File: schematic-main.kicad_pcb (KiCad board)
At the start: 2 copper layers, 107 parts, among them IC1 AD8544ARUZ-REEL, IC2 LM76202QPWPRQ1, J1 Battery, J2 CAN, J3 V_P, J7 C_P, J8 VALVE, J9 PURGE_VALVE, P1 USB_C_Plug_USB2.0, T1 PMPB15XP_115, U2 TPS62933, U3 USBLC6-2P6, U4 ESP32-S3FN8, U5 SN65HVD232, Y1 Crystal_GND24

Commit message: Drawing PCB
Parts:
- moved R26 200.8 mm to (70.4, 158.5), turned to -90 degrees
- moved IC1 196.7 mm to (76.5, 157.7), turned to 180 degrees
- moved U2 193.4 mm to (68.5, 107.8)
- moved D2 192.2 mm to (64.6, 100.9), turned to 90 degrees
- moved R22 187.5 mm to (73.8, 83.2), turned to 180 degrees
- moved L1 186.3 mm to (76.0, 107.5), turned to 90 degrees
- moved R9 182.0 mm to (69.6, 96.4), turned to 180 degrees
- moved R17 180.9 mm to (83.3, 151.1), turned to 90 degrees
- moved R29 180.1 mm to (94.5, 138.2), turned to 90 degrees
- moved C30 179.8 mm to (73.6, 152.2), turned to 90 degrees
- moved C3 178.0 mm to (65.2, 109.5), turned to -90 degrees
- moved R16 176.6 mm to (84.8, 155.0), turned to 180 degrees
- moved D6 176.5 mm to (79.2, 83.2)
- moved R7 175.9 mm to (74.6, 96.4), turned to 180 degrees
- moved C26 175.4 mm to (79.4, 152.2), turned to 90 degrees
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- renumbered T1 to MOSFET1
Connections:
- D3 pad 1: /IO/CANH -> /IO/CANL
- D3 pad 2: /IO/CANL -> /IO/CANH
- U4 pad 12: /I/O_1_MCU -> unconnected-(U4-GPIO7/ADC1_CH6-Pad12)
- U4 pad 13: /I/O_2_MCU -> unconnected-(U4-GPIO8/ADC1_CH7-Pad13)
- U4 pad 14: /I/O_3_MCU -> unconnected-(U4-GPIO9/ADC1_CH8-Pad14)
- U4 pad 15: /I/O_4_MCU -> unconnected-(U4-GPIO10/ADC1_CH9-Pad15)
- U4 pad 18: /V_P_MCU -> unconnected-(U4-GPIO13/ADC2_CH2-Pad18)
- U4 pad 19: /PURGE_VALVE_MCU -> unconnected-(U4-GPIO14/ADC2_CH3-Pad19)
- U4 pad 23: unconnected-(U4-GPIO17/ADC2_CH6-Pad23) -> /V_P_MCU
- U4 pad 24: unconnected-(U4-GPIO18/ADC2_CH7-Pad24) -> /C_P_MCU
- U4 pad 39: unconnected-(U4-GPIO34-Pad39) -> /I/O_1_MCU
- U4 pad 40: unconnected-(U4-GPIO35-Pad40) -> /I/O_2_MCU
- U4 pad 41: unconnected-(U4-GPIO36-Pad41) -> /I/O_3_MCU
- U4 pad 42: unconnected-(U4-GPIO37-Pad42) -> /I/O_4_MCU
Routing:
- net GND: track 0.00 -> 604.2 mm, vias 0 -> 57
- net +12V: track 0.00 -> 274.8 mm
- net +3.3V: track 0.00 -> 248.3 mm, vias 0 -> 7
- net /MCU/MCU_TEST: track 0.00 -> 100.5 mm, vias 0 -> 2
- net /MCU/BOOT: track 0.00 -> 95.2 mm, vias 0 -> 2
- net /VBUS: track 0.00 -> 95.1 mm, vias 0 -> 2
- net /MCU/RESET: track 0.00 -> 90.4 mm, vias 0 -> 2
- net /MCU/USB_D+: track 0.00 -> 58.7 mm, vias 0 -> 2
- net /MCU/USB_D-: track 0.00 -> 56.7 mm
- net /I/O_4_MCU: track 0.00 -> 47.4 mm, vias 0 -> 2
- net /I/O_3_MCU: track 0.00 -> 42.2 mm, vias 0 -> 2
- net /IO/VALVE: track 0.00 -> 39.3 mm
- net /IO/PURGE_VALVE: track 0.00 -> 39.1 mm
- net /I/O_2_MCU: track 0.00 -> 37.5 mm, vias 0 -> 2
- net +5V: track 0.00 -> 37.0 mm
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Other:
- board outline added: 102.3 x 135.4 mm
- board text added: "12V"
- board text added: "3.3V"
- board text added: "5V"
- board text added: "BOOT"
- board text added: "CAN_STATUS"
- board text added: "GND"
- board text added: "I/O_1"
- board text added: "I/O_2"
- board text added: "I/O_3"
- board text added: "I/O_4"
- board text added: "MCU_STATUS"
- board text added: "MCU_TEST"
- board text added: "RESET"

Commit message: Makin GND sphere
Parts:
- added H1: MountingHole, MountingHole:MountingHole_3.2mm_M3_DIN965, F.Cu at (146.8, 51.8)
- added H2: MountingHole, MountingHole:MountingHole_3.2mm_M3_DIN965, F.Cu at (53.6, 51.8)
- added H3: MountingHole, MountingHole:MountingHole_3.2mm_M3_DIN965, F.Cu at (53.4, 178.4)
- added H4: MountingHole, MountingHole:MountingHole_3.2mm_M3_DIN965, F.Cu at (146.8, 178.6)
- moved C25 7.80 mm to (139.7, 177.6)
- moved JP3 7.80 mm to (140.4, 180.4)
- moved R23 7.80 mm to (139.8, 174.9)
- moved C13 4.60 mm to (133.0, 177.6)
- moved JP2 4.60 mm to (133.9, 180.4)
- moved R13 4.60 mm to (133.0, 174.9)
- moved TP3 3.20 mm to (141.2, 59.4)
- moved TP4 3.20 mm to (148.1, 59.4)
- moved C12 2.47 mm to (126.2, 177.6)
- moved R12 2.47 mm to (126.2, 174.9)
- moved JP1 2.47 mm to (127.0, 180.5)
- moved C10 1.50 mm to (105.8, 114.8)
- moved TP5 1.50 mm to (141.1, 65.2)
- moved TP6 1.50 mm to (148.1, 65.2)
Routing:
- net /C_P_MCU: track 2.74 -> 73.2 mm, vias 0 -> 2
- net /V_P_MCU: track 2.74 -> 67.7 mm, vias 0 -> 2
- net /MCU/MCU_TEST: track 100.5 -> 93.6 mm
- net GND: track 604.2 -> 609.7 mm, vias 57 -> 59
- net /MCU/BOOT: track 95.2 -> 90.8 mm
- net +3.3V: track 248.3 -> 251.2 mm, vias 7 -> 10
- net +12V: track 274.8 -> 272.0 mm
- net /MCU/RESET: track 90.4 -> 89.6 mm
- net +5V: track 37.0 -> 36.4 mm
- added copper zone on B.Cu, net GND
- added copper zone on F.Cu, net GND

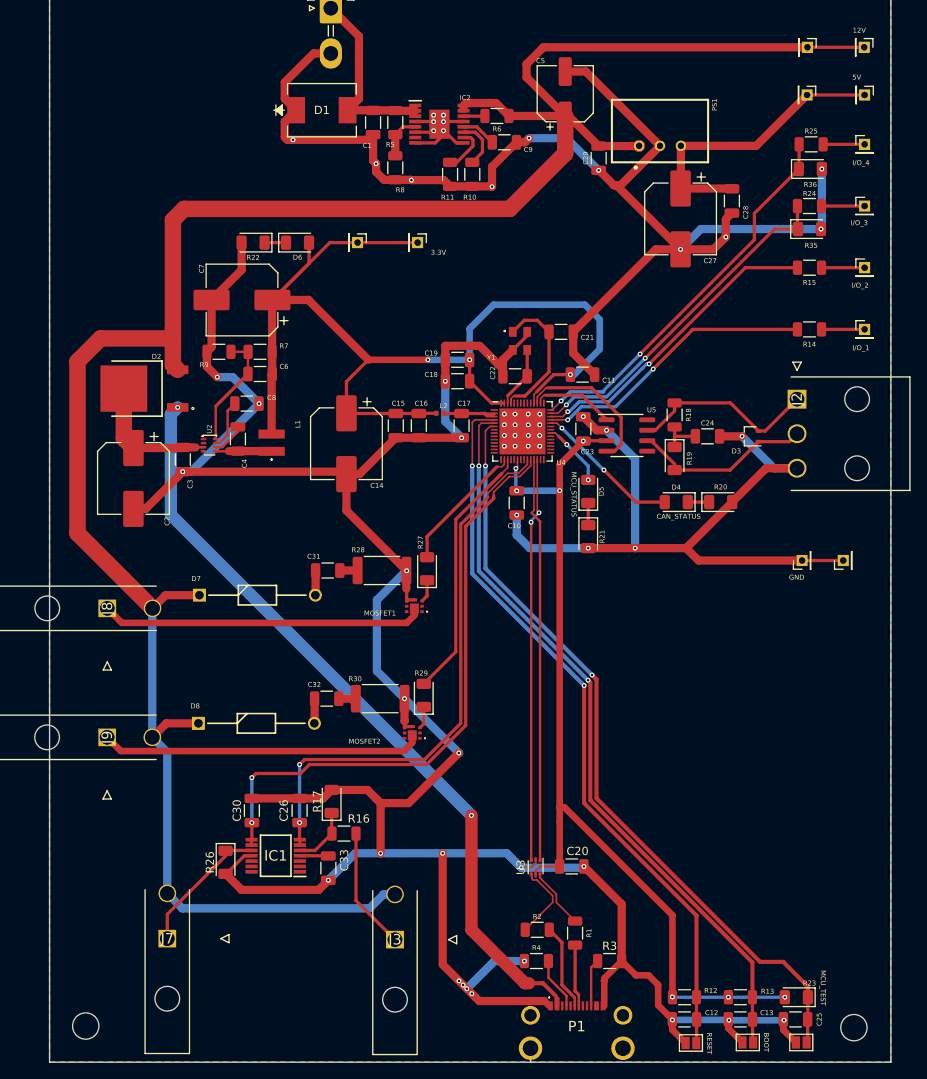
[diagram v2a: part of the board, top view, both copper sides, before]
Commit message: Adding connector for Hydrogen Sensor
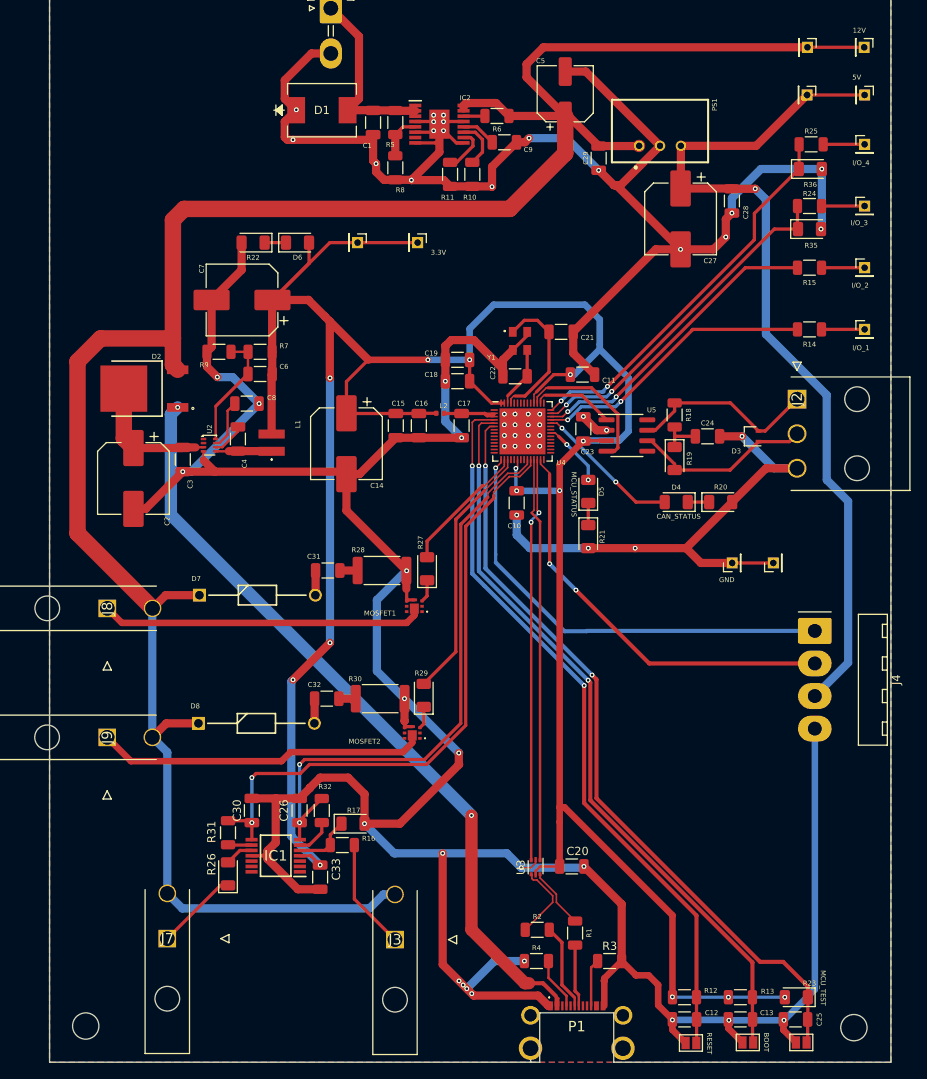
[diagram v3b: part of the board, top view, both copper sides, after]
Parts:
- added J4: Conn_01x04, Connector_Molex:Molex_KK-396_A-41792-0004_1x04_P3.96mm_Horizontal, F.Cu at (142.0, 130.4)
- added R31: 1k, Resistor_SMD:R_1206_3216Metric, F.Cu at (70.7, 154.9)
- added R32: 1k, Resistor_SMD:R_1206_3216Metric, F.Cu at (82.1, 152.2)
- R16: value 10k -> 5k
- R17: value 5k -> 10k
- R26: value 100R -> 150R
- moved TP1 8.51 mm to (132.0, 122.1)
- moved TP2 8.51 mm to (137.0, 122.1)
- moved R17 3.75 mm to (85.9, 153.8), turned to 0 degrees
- moved C33 1.49 mm to (81.9, 160.3)
- moved R26 1.43 mm to (70.7, 159.9), turned to 90 degrees
- moved R16 1.41 mm to (84.6, 156.4)
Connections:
- net /IO/V_P renamed /IO/PRESSURE_SENSOR_V
- C26 pad 1: /V_P_MCU -> /PRESSURE_SENSOR_V_MCU
- C30 pad 1: /C_P_MCU -> /PRESSURE_SENSOR_I_MCU
- IC1 pad 10: /IO/C_P -> Net-(IC1-+IN_C)
- IC1 pad 6: /V_P_MCU -> Net-(IC1--IN_B)
- IC1 pad 7: /V_P_MCU -> /PRESSURE_SENSOR_V_MCU
- IC1 pad 8: /C_P_MCU -> /PRESSURE_SENSOR_I_MCU
- IC1 pad 9: /C_P_MCU -> Net-(IC1--IN_C)
- J7 pad 1: /IO/C_P -> /IO/PRESSURE_SENSOR_I
- R26 pad 1: /IO/C_P -> /IO/PRESSURE_SENSOR_I
- R26 pad 2: GND -> Net-(IC1-+IN_C)
- U4 pad 15: unconnected-(U4-GPIO10/ADC1_CH9-Pad15) -> /HYDROGEN_SENSOR_ADC
- U4 pad 23: /V_P_MCU -> /PRESSURE_SENSOR_V_MCU
- U4 pad 24: /C_P_MCU -> /PRESSURE_SENSOR_I_MCU
- U4 pad 27: unconnected-(U4-GPIO21-Pad27) -> /HYDROGEN_SENSOR_
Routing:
- net +3.3V: track 251.2 -> 337.5 mm, vias 10 -> 14
- net /PRESSURE_SENSOR_I_MCU: track 0.00 -> 75.5 mm, vias 0 -> 2
- net /C_P_MCU: track 73.2 -> 0.00 mm, vias 2 -> 0
- net /PRESSURE_SENSOR_V_MCU: track 0.00 -> 71.1 mm, vias 0 -> 2
- net +5V: track 36.4 -> 107.2 mm, vias 0 -> 1
- net /V_P_MCU: track 67.7 -> 0.00 mm, vias 2 -> 0
- net /HYDROGEN_SENSOR_ADC: track 0.00 -> 55.1 mm, vias 0 -> 1
- net /HYDROGEN_SENSOR_: track 0.00 -> 50.4 mm, vias 0 -> 2
- net GND: track 609.7 -> 627.8 mm, vias 59 -> 60
- net /IO/C_P: track 16.8 -> 0.00 mm
- net /IO/PRESSURE_SENSOR_I: track 0.00 -> 10.1 mm
- net Net-(IC1--IN_B): track 0.00 -> 4.51 mm
- net Net-(IC1-+IN_C): track 0.00 -> 3.46 mm
- net Net-(IC1--IN_C): track 0.00 -> 2.88 mm
- net /IO/PRESSURE_SENSOR_V: track 14.9 -> 13.5 mm
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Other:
- outline, holes or cut-outs redrawn

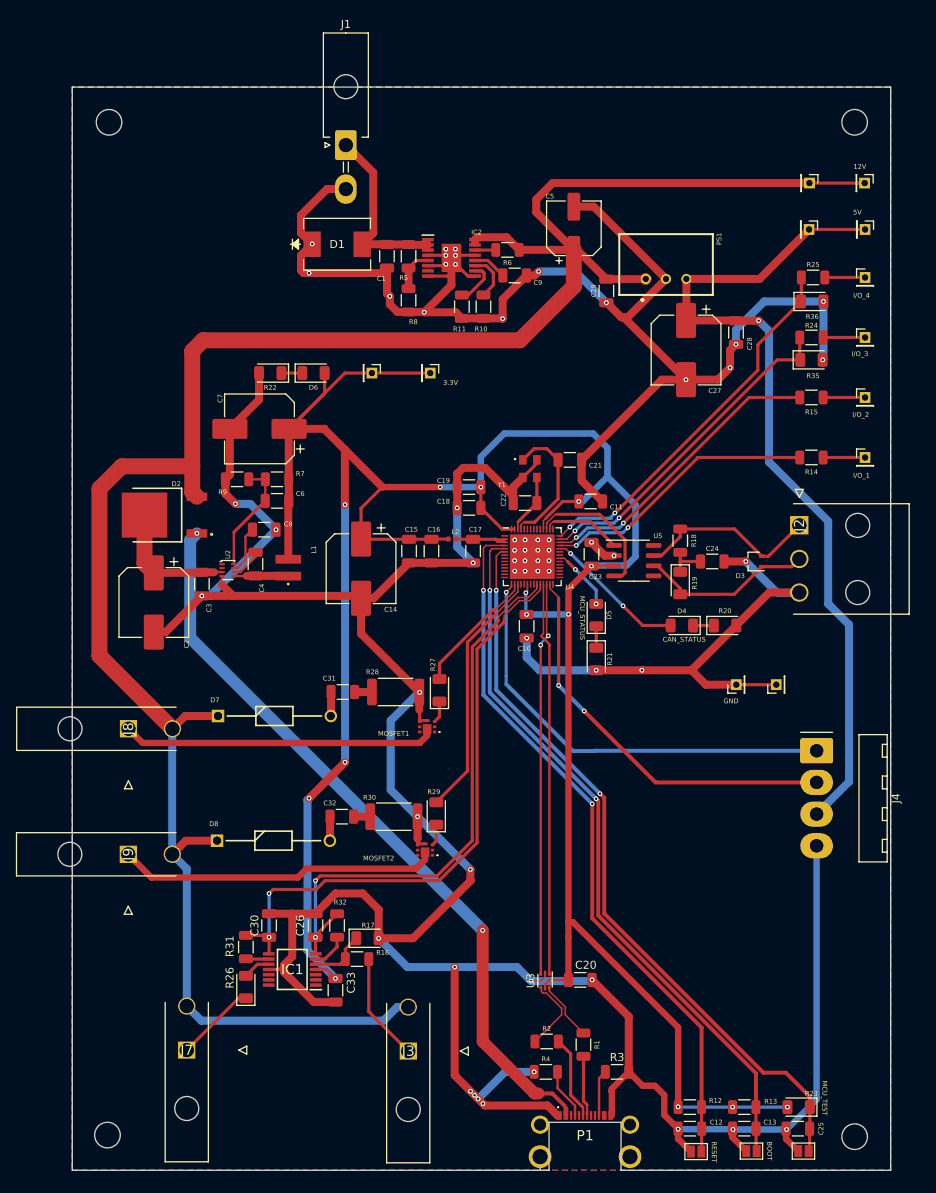
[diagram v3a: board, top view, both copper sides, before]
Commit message: Adding motor driver unit
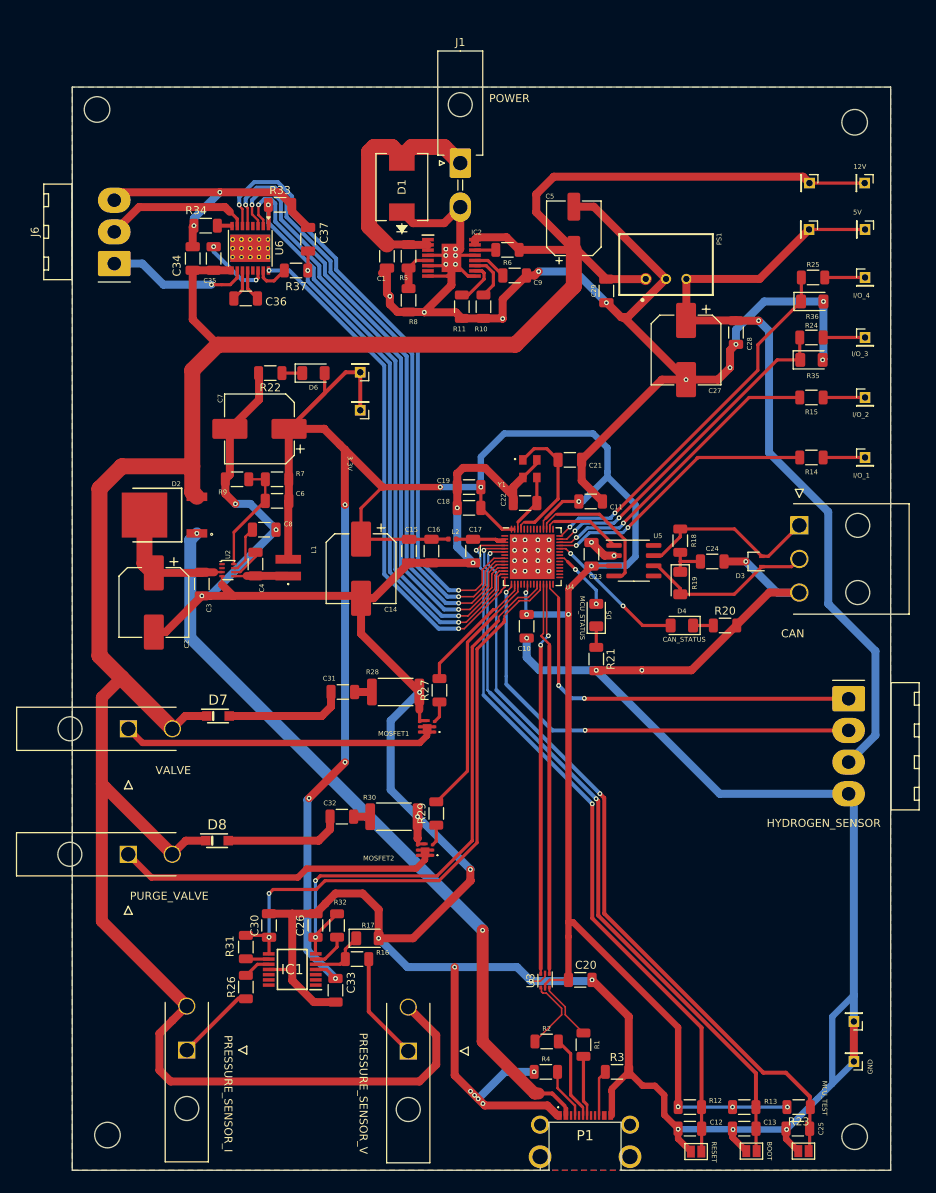
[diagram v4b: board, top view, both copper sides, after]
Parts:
- added C34: 100n, Capacitor_SMD:C_1206_3216Metric, F.Cu at (64.1, 68.8)
- added C35: 100n, Capacitor_SMD:C_1206_3216Metric, F.Cu at (66.7, 68.8)
- added C36: 100n, Capacitor_SMD:C_1206_3216Metric, F.Cu at (70.7, 73.8)
- added C37: 1n, Capacitor_SMD:C_1206_3216Metric, F.Cu at (78.5, 66.4)
- added J6: MOTOR_DRIVER, Connector_Molex:Molex_KK-396_A-41792-0003_1x03_P3.96mm_Horizontal, F.Cu at (54.3, 69.5)
- added R33: 10k, Resistor_SMD:R_1206_3216Metric, F.Cu at (75.0, 62.1)
- added R34: 0.2, Resistor_SMD:R_1206_3216Metric, F.Cu at (65.7, 64.7)
- added R37: 100k, Resistor_SMD:R_1206_3216Metric, F.Cu at (77.0, 70.3)
- added U6: DRV8801PWP, Package_SO:HTSSOP-16-1EP_4.4x5mm_P0.65mm_EP3.4x5mm_Mask3x3mm_ThermalVias, F.Cu at (71.2, 67.5)
- D7, D8: footprint Diode_SMD:DIOAD1414W86L464D238 -> Diode_SMD:PMEG10020ELR
- R20, R21, R22, R23, R26, R27, R29: footprint LED_SMD:LED_1206_3216Metric -> Resistor_SMD:R_1206_3216Metric
- moved TP1 49.3 mm to (146.7, 169.2), turned to 180 degrees
- moved TP2 43.2 mm to (146.7, 164.2), turned to 180 degrees
- moved J1 14.5 mm to (97.5, 56.9)
- moved D1 10.8 mm to (90.2, 59.9), turned to 90 degrees
- moved TP7 9.91 mm to (85.0, 87.8), turned to 180 degrees
- moved J4 7.63 mm to (146.0, 123.9)
- moved H2 2.19 mm to (52.1, 50.2)
- moved TP8 1.45 mm to (85.0, 83.0), turned to 180 degrees
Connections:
- J4 pad 1: /HYDROGEN_SENSOR_ADC -> /HYDROGEN_SENSOR_
- J4 pad 2: /HYDROGEN_SENSOR_ -> /HYDROGEN_SENSOR_ADC
- MOSFET1 pad 1: unconnected-(MOSFET1-Pad1) -> /IO/VALVE
- MOSFET1 pad 2: unconnected-(MOSFET1-Pad2) -> /IO/VALVE
- MOSFET1 pad 5: unconnected-(MOSFET1-Pad5) -> /IO/VALVE
- MOSFET1 pad 6: unconnected-(MOSFET1-Pad6) -> /IO/VALVE
- MOSFET2 pad 1: unconnected-(MOSFET2-Pad1) -> /IO/PURGE_VALVE
- MOSFET2 pad 2: unconnected-(MOSFET2-Pad2) -> /IO/PURGE_VALVE
- MOSFET2 pad 5: unconnected-(MOSFET2-Pad5) -> /IO/PURGE_VALVE
- MOSFET2 pad 6: unconnected-(MOSFET2-Pad6) -> /IO/PURGE_VALVE
- U4 pad 10: unconnected-(U4-GPIO5/ADC1_CH4-Pad10) -> /DIRECTION_MOTOR
- U4 pad 11: unconnected-(U4-GPIO6/ADC1_CH5-Pad11) -> /DECAY_MODE_MOTOR
- U4 pad 12: unconnected-(U4-GPIO7/ADC1_CH6-Pad12) -> /FAULT_MOTOR
- U4 pad 13: unconnected-(U4-GPIO8/ADC1_CH7-Pad13) -> /ADC_MOTOR
- U4 pad 14: unconnected-(U4-GPIO9/ADC1_CH8-Pad14) -> /DRIVER_SIDE
- U4 pad 8: unconnected-(U4-GPIO3/ADC1_CH2-Pad8) -> /ENABLE_MOTOR
- U4 pad 9: unconnected-(U4-GPIO4/ADC1_CH3-Pad9) -> /SLEEP_MOTOR
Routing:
- net /ENABLE_MOTOR: track 0.00 -> 78.9 mm, vias 0 -> 2
- net /SLEEP_MOTOR: track 0.00 -> 77.9 mm, vias 0 -> 2
- net /DIRECTION_MOTOR: track 0.00 -> 77.1 mm, vias 0 -> 2
- net /DECAY_MODE_MOTOR: track 0.00 -> 75.8 mm, vias 0 -> 2
- net /FAULT_MOTOR: track 0.00 -> 74.3 mm, vias 0 -> 2
- net GND: track 627.8 -> 700.5 mm
- net /DRIVER_SIDE: track 0.00 -> 66.8 mm, vias 0 -> 2
- net /ADC_MOTOR: track 0.00 -> 64.8 mm, vias 0 -> 2
- net +12V: track 272.0 -> 332.6 mm
- net /IO_2/+MOTOR: track 0.00 -> 18.2 mm
- net /IO_2/-MOTOR: track 0.00 -> 17.7 mm, vias 0 -> 1
- net Net-(D7-A): track 3.01 -> 15.0 mm
- net Net-(D8-A): track 3.01 -> 14.9 mm
- net /Power /Vin: track 23.9 -> 33.1 mm
- net Net-(U6-VCP): track 0.00 -> 8.70 mm, vias 0 -> 2
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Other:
- board text added: "CAN"
- board text added: "HYDROGEN_SENSOR"
- board text added: "POWER"
- board text added: "PRESSURE_SENSOR_I"
- board text added: "PRESSURE_SENSOR_V"
- board text added: "PURGE_VALVE"
- board text added: "VALVE"

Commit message: Change of dimensions
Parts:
- removed J6: MOTOR_DRIVER, Connector_Molex:Molex_KK-396_A-41792-0003_1x03_P3.96mm_Horizontal
- added J10: Motor, Connector_Molex:Molex_Mini-Fit_Jr_5569-02A2_2x01_P4.20mm_Horizontal, F.Cu at (52.6, 76.2)
- moved JP1 67.8 mm to (67.9, 147.2)
- moved C12 67.8 mm to (67.1, 144.3)
- moved C13 67.8 mm to (73.9, 144.3)
- moved JP2 67.8 mm to (74.8, 147.1)
- moved JP3 67.8 mm to (81.3, 147.1)
- moved R12 67.8 mm to (67.1, 141.6)
- moved R13 67.8 mm to (73.9, 141.6)
- moved R23 67.8 mm to (80.7, 141.6)
- moved C25 67.8 mm to (80.6, 144.3)
- moved J7 54.6 mm to (112.6, 144.3)
- moved C30 53.0 mm to (121.1, 128.8)
- moved C33 53.0 mm to (129.4, 136.9)
- moved R16 53.0 mm to (132.1, 133.0)
- moved R17 53.0 mm to (133.4, 130.4)
- moved R26 53.0 mm to (118.2, 136.5)
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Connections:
- C31 pad 1: Net-(D7-A) -> /IO/VALVE
- C32 pad 1: Net-(D8-A) -> /IO/PURGE_VALVE
- D7 pad 2: Net-(D7-A) -> /IO/VALVE
- D8 pad 2: Net-(D8-A) -> /IO/PURGE_VALVE
- U4 pad 23: /PRESSURE_SENSOR_V_MCU -> /PRESSURE_SENSOR_I_MCU
- U4 pad 24: /PRESSURE_SENSOR_I_MCU -> /PRESSURE_SENSOR_V_MCU
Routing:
- net GND: track 700.5 -> 551.9 mm, vias 60 -> 55
- net /MCU/MCU_TEST: track 95.1 -> 54.0 mm
- net +3.3V: track 333.6 -> 295.0 mm, vias 14 -> 16
- net /PRESSURE_SENSOR_I_MCU: track 75.5 -> 40.2 mm, vias 2 -> 1
- net /MCU/BOOT: track 91.9 -> 57.6 mm
- net /Power /Vin: track 33.1 -> 65.1 mm
- net /MCU/RESET: track 90.7 -> 62.6 mm
- net +5V: track 101.8 -> 78.9 mm
- net /MCU/USB_D-: track 56.7 -> 35.3 mm, vias 0 -> 2
- net /MCU/USB_D+: track 58.7 -> 37.9 mm
- net /IO/VALVE: track 43.5 -> 64.2 mm
- net /PRESSURE_SENSOR_V_MCU: track 71.1 -> 50.5 mm, vias 2 -> 3
- net /IO/PURGE_VALVE: track 44.4 -> 63.0 mm
- net Net-(D7-A): track 15.0 -> 0.00 mm
- net Net-(D8-A): track 14.9 -> 0.00 mm
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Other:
- board size 102.3 x 135.4 mm -> 100 x 99.9 mm
- board text added: "Fuel Cell Unit v1 Michał Borkowski 05.03.2024"
- board text removed: "CAN"
